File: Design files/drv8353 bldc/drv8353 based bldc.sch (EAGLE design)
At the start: 121 parts, among them J4 B06B-HCMKK, Q1 FDBL86062-F085, Q2 FDBL86062-F085, Q3 FDBL86062-F085, Q4 FDBL86062-F085, Q5 FDBL86062-F085, Q6 FDBL86062-F085, U1 Value

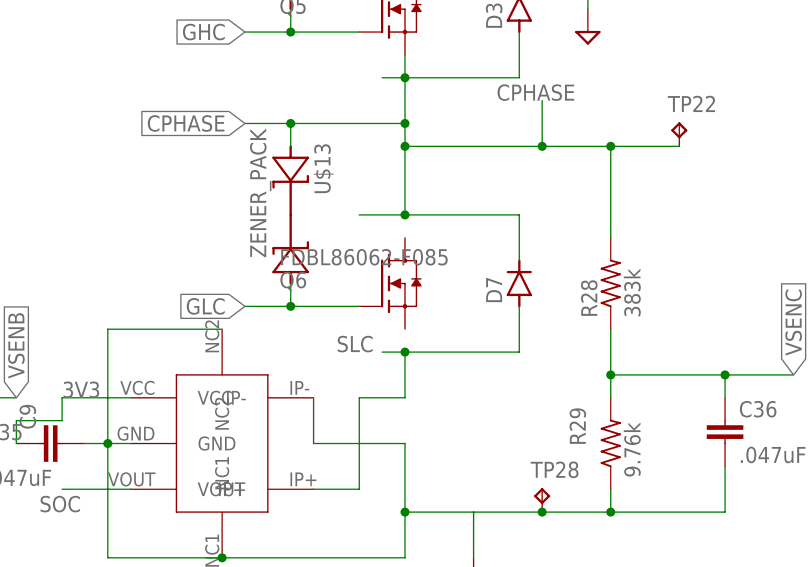
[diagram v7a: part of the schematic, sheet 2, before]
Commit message: adds space for larger fets
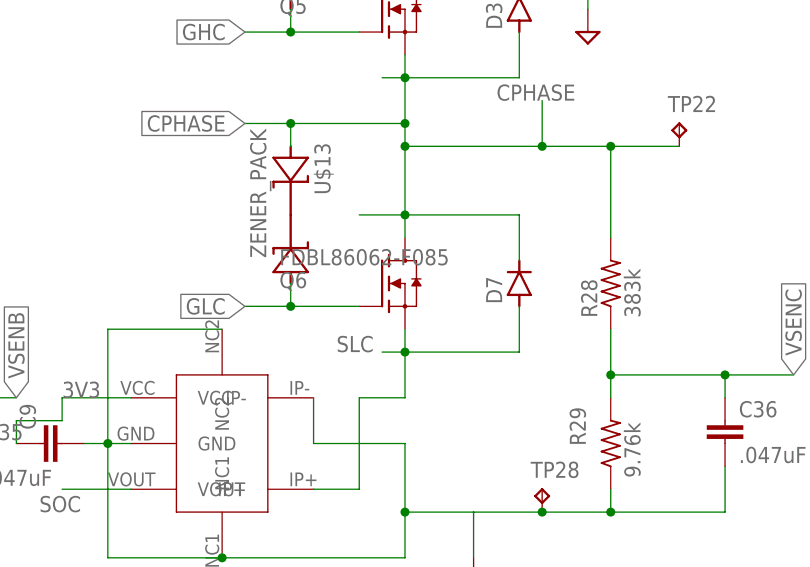
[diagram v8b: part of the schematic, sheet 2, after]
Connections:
- net CPHASE: now also Q6.D
- net SLC: now also Q6.S
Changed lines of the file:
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@@
 <wire x1="99.06" y1="7.62" x2="99.06" y2="17.78" width="0.1524" layer="91"/>
 <wire x1="99.06" y1="17.78" x2="104.14" y2="17.78" width="0.1524" layer="91"/>
+<pinref part="Q6" gate="G$1" pin="S"/>
+<wire x1="104.14" y1="25.4" x2="104.14" y2="22.86" width="0.1524" layer="91"/>
 </segment>
 </net>
@@
 <wire x1="91.44" y1="45.72" x2="91.44" y2="48.26" width="0.1524" layer="91"/>
 <junction x="91.44" y="48.26"/>
+<pinref part="Q6" gate="G$1" pin="D"/>
+<wire x1="104.14" y1="35.56" x2="104.14" y2="38.1" width="0.1524" layer="91"/>
 </segment>
 </net>
